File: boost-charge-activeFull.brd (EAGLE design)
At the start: 28.6 x 21.9 mm, 20 parts, among them U1 MCP73831

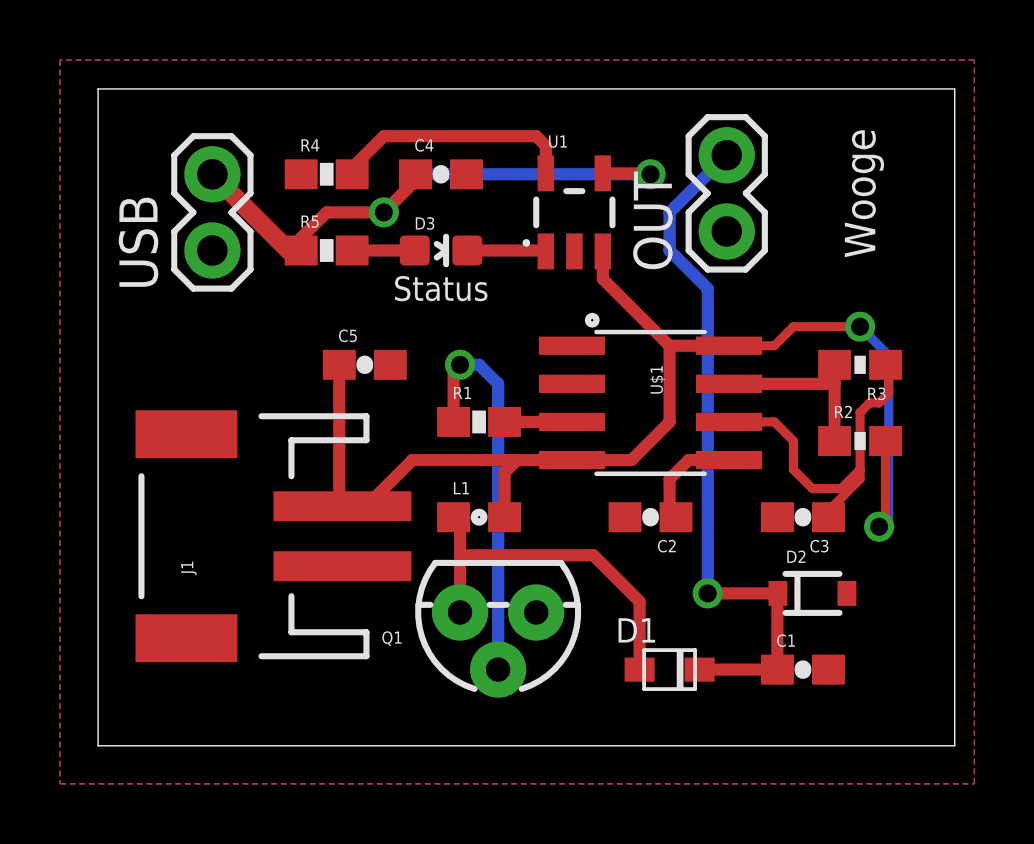
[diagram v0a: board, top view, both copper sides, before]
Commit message: Connected trigger
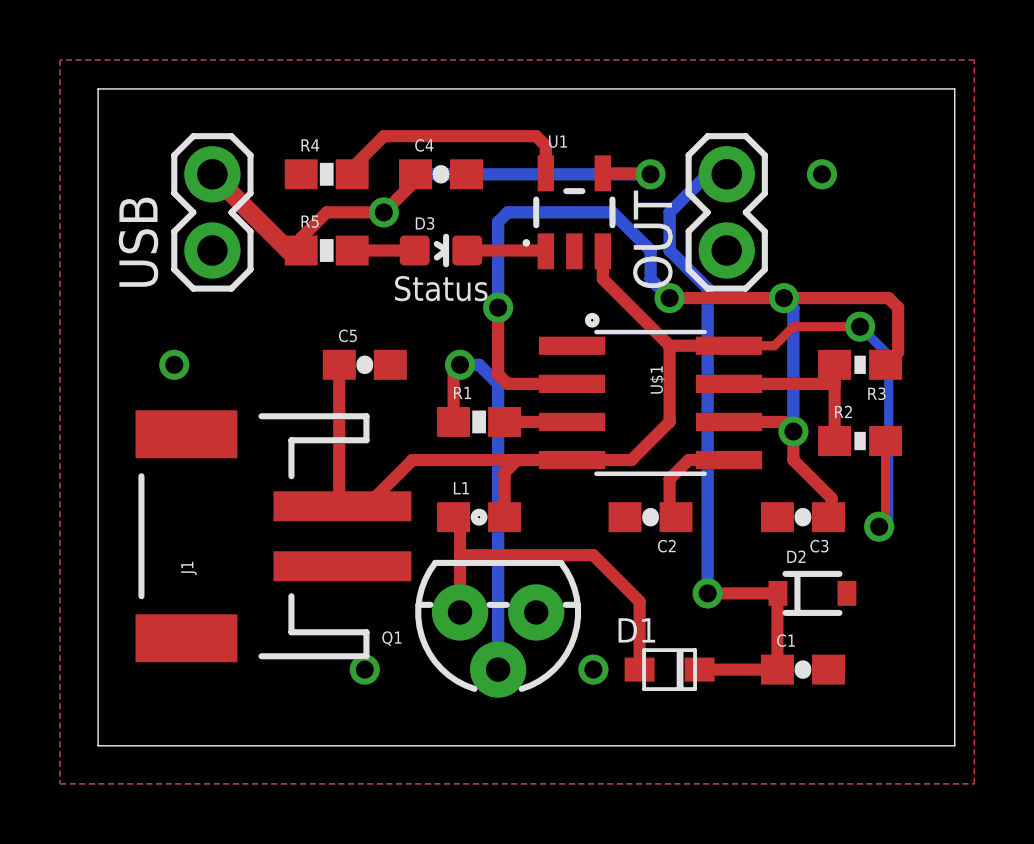
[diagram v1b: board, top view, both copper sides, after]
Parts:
- moved OUT 0.63 mm to (21.0, 16.5)
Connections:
- removed net N$6: C3.1, R3.1, U$1.6
- net N$5: now also C3.1, R3.1, U$1.6
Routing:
- net N$5: track 0.00 -> 35.4 mm, vias 0 -> 4
- net N$6: track 12.3 -> 0.00 mm
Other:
- board text added: "I am a Fucking genius"
- board text removed: "10/17/15"
- board text removed: "Wooge"
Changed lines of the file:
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@@
 9vBoost</text>
 <text x="11.43" y="15.24" size="0.8128" layer="21" align="center">Status</text>
-<text x="25.4" y="18.415" size="1.016" layer="21" rot="R270" align="center">Wooge</text>
-<text x="24.765" y="2.2225" size="1.016" layer="22" rot="MR0" align="center">10/17/15</text>
+<text x="1.905" y="10.795" size="1.016" layer="22" font="vector" rot="MR90" align="center">I am a Fucking genius</text>
 </plain>
 <attributes>
@@
 <attribute name="TOP_NEG" value="-" x="4.445" y="6.985" size="1.778" layer="27" rot="R90" display="off"/>
 </element>
-<element name="OUT" library="SparkFun-Connectors" package="1X02" value="" x="20.955" y="17.145" rot="R90"/>
+<element name="OUT" library="SparkFun-Connectors" package="1X02" value="" x="20.955" y="16.51" rot="R90"/>
 <element name="L1" library="SparkFun-Passives" package="0603" value="" x="12.7" y="7.62"/>
 <element name="Q1" library="SparkFun-DiscreteSemi" package="TO-92" value="" x="13.335" y="4.445" rot="R180">
@@
 <contactref element="U1" pad="2"/>
 <contactref element="C5" pad="2"/>
+<via x="24.13" y="19.05" extent="1-16" drill="0.6"/>
+<via x="2.54" y="12.7" extent="1-16" drill="0.6"/>
+<via x="16.51" y="2.54" extent="1-16" drill="0.6"/>
+<via x="8.89" y="2.54" extent="1-16" drill="0.6"/>
 </signal>
 <signal name="3V">
@@
 <wire x1="20.32" y1="15.24" x2="19.05" y2="16.51" width="0.4064" layer="16"/>
 <wire x1="19.05" y1="16.51" x2="19.05" y2="17.78" width="0.4064" layer="16"/>
-<wire x1="19.05" y1="17.78" x2="20.955" y2="19.685" width="0.4064" layer="16"/>
+<wire x1="19.05" y1="17.78" x2="20.32" y2="19.05" width="0.4064" layer="16"/>
+<wire x1="20.32" y1="19.05" x2="20.955" y2="19.05" width="0.4064" layer="16"/>
 </signal>
 <signal name="N$2">
@@
 <signal name="N$5">
 <contactref element="U$1" pad="2"/>
-</signal>
-<signal name="N$6">
+<contactref element="R3" pad="1"/>
 <contactref element="U$1" pad="6"/>
-<contactref element="R3" pad="1"/>
 <contactref element="C3" pad="1"/>
-<wire x1="24.345" y1="7.62" x2="24.345" y2="7.835" width="0.3048" layer="1"/>
-<wire x1="24.345" y1="7.835" x2="25.4" y2="8.89" width="0.3048" layer="1"/>
-<wire x1="25.4" y1="8.89" x2="25.4" y2="9.2075" width="0.3048" layer="1"/>
-<wire x1="25.4" y1="9.2075" x2="25.4" y2="11.1125" width="0.3048" layer="1"/>
-<wire x1="25.4" y1="11.1125" x2="25.7175" y2="11.43" width="0.3048" layer="1"/>
-<wire x1="25.7175" y1="11.43" x2="26.035" y2="11.43" width="0.3048" layer="1"/>
-<wire x1="26.035" y1="11.43" x2="26.3525" y2="11.7475" width="0.3048" layer="1"/>
-<wire x1="26.3525" y1="11.7475" x2="26.3525" y2="12.5975" width="0.3048" layer="1"/>
-<wire x1="26.3525" y1="12.5975" x2="26.25" y2="12.7" width="0.3048" layer="1"/>
-<wire x1="21.0312" y1="10.795" x2="22.5425" y2="10.795" width="0.3048" layer="1"/>
-<wire x1="22.5425" y1="10.795" x2="23.1775" y2="10.16" width="0.3048" layer="1"/>
-<wire x1="23.1775" y1="10.16" x2="23.1775" y2="9.2075" width="0.3048" layer="1"/>
-<wire x1="23.1775" y1="9.2075" x2="23.8125" y2="8.5725" width="0.3048" layer="1"/>
-<wire x1="23.8125" y1="8.5725" x2="24.765" y2="8.5725" width="0.3048" layer="1"/>
-<wire x1="24.765" y1="8.5725" x2="25.4" y2="9.2075" width="0.3048" layer="1"/>
+<wire x1="15.7988" y1="12.065" x2="13.6525" y2="12.065" width="0.4064" layer="1"/>
+<wire x1="13.6525" y1="12.065" x2="13.335" y2="12.3825" width="0.4064" layer="1"/>
+<wire x1="13.335" y1="12.3825" x2="13.335" y2="14.605" width="0.4064" layer="1"/>
+<via x="13.335" y="14.605" extent="1-16" drill="0.6"/>
+<wire x1="13.335" y1="14.605" x2="13.335" y2="17.4625" width="0.4064" layer="16"/>
+<wire x1="13.335" y1="17.4625" x2="13.6525" y2="17.78" width="0.4064" layer="16"/>
+<wire x1="13.6525" y1="17.78" x2="17.145" y2="17.78" width="0.4064" layer="16"/>
+<wire x1="17.145" y1="17.78" x2="18.415" y2="16.51" width="0.4064" layer="16"/>
+<wire x1="18.415" y1="16.51" x2="18.415" y2="15.5575" width="0.4064" layer="16"/>
+<wire x1="18.415" y1="15.5575" x2="19.05" y2="14.9225" width="0.4064" layer="16"/>
+<via x="19.05" y="14.9225" extent="1-16" drill="0.6"/>
+<wire x1="19.05" y1="14.9225" x2="22.86" y2="14.9225" width="0.4064" layer="1"/>
+<wire x1="22.86" y1="14.9225" x2="26.3525" y2="14.9225" width="0.4064" layer="1"/>
+<wire x1="26.3525" y1="14.9225" x2="26.67" y2="14.605" width="0.4064" layer="1"/>
+<wire x1="26.67" y1="14.605" x2="26.67" y2="13.12" width="0.4064" layer="1"/>
+<wire x1="26.67" y1="13.12" x2="26.25" y2="12.7" width="0.4064" layer="1"/>
+<wire x1="21.0312" y1="10.795" x2="22.86" y2="10.795" width="0.4064" layer="1"/>
+<wire x1="22.86" y1="10.795" x2="23.1775" y2="10.4775" width="0.4064" layer="1"/>
+<wire x1="23.1775" y1="10.4775" x2="23.1775" y2="9.525" width="0.4064" layer="1"/>
+<wire x1="23.1775" y1="9.525" x2="24.4475" y2="8.255" width="0.4064" layer="1"/>
+<wire x1="24.4475" y1="8.255" x2="24.4475" y2="7.7225" width="0.4064" layer="1"/>
+<wire x1="24.4475" y1="7.7225" x2="24.345" y2="7.62" width="0.4064" layer="1"/>
+<via x="23.1775" y="10.4775" extent="1-16" drill="0.6"/>
+<wire x1="23.1775" y1="10.4775" x2="23.1775" y2="14.605" width="0.4064" layer="16"/>
+<wire x1="23.1775" y1="14.605" x2="22.86" y2="14.9225" width="0.4064" layer="16"/>
+<via x="22.86" y="14.9225" extent="1-16" drill="0.6"/>
 </signal>
 <signal name="N$7">
